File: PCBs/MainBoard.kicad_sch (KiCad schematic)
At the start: 37 parts, among them IC1 PASCO2V01BUMA1, J1 Conn_01x12_FPC_0.5mm, J4 SM06B-GHS-TB, J5 USB_C_Receptacle, SW1 SMD_4.6x2.8mm_h2.5mm, SW2 SMD_4.6x2.8mm_h2.5mm, SW3 PTH_RA_h7.5mm, U1 AP3012, U2 ESP32-S3-WROOM-1-N16R2, U5 AP2112K-3.3

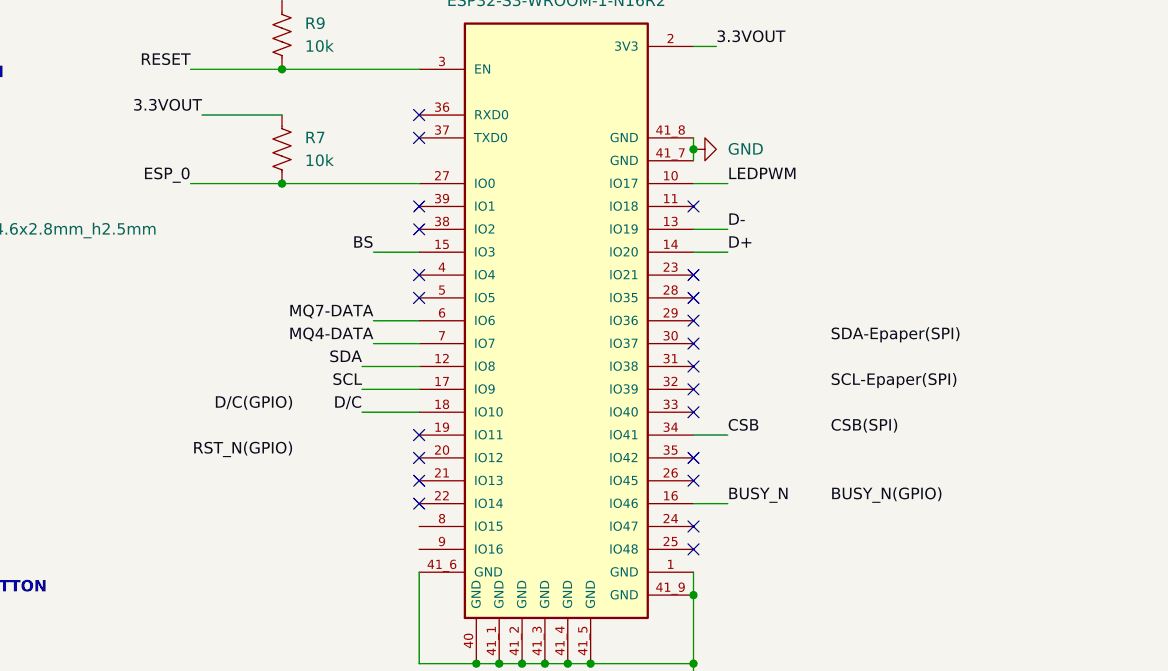
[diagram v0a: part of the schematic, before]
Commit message: Updated main board
Updated connections for Epaper discplay
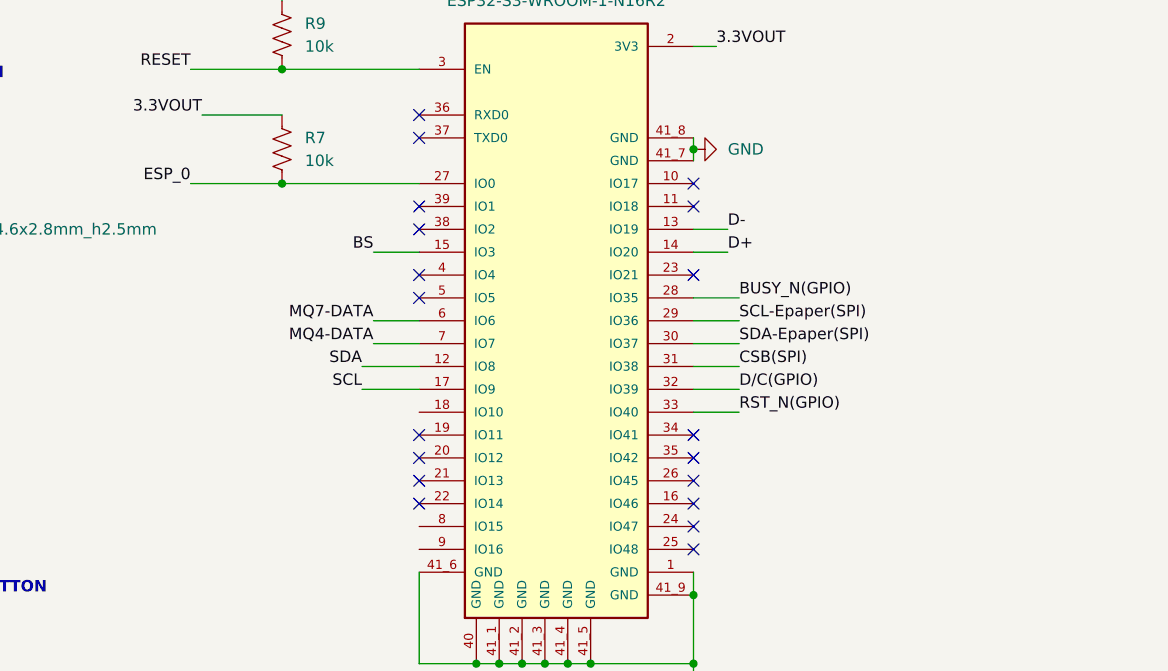
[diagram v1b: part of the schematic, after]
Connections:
- net BUSY_N(GPIO): now also U2.28 (IO35)
- net CSB(SPI): now also U2.31 (IO38)
- net D/C(GPIO): now also U2.32 (IO39)
- net RST_N(GPIO): now also U2.33 (IO40)
- net SCL-Epaper(SPI): now also U2.29 (IO36)
- net SDA-Epaper(SPI): now also U2.30 (IO37)
- net BUSY_N: no longer names the net of U2.16 (IO46)
- net CSB: no longer names the net of U2.34 (IO41)
- net D/C: no longer names the net of U2.18 (IO10)
- net LEDPWM: no longer names the net of U2.10 (IO17)
- no-connect marks 35 -> 32
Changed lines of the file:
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@@
   (no_connect (at 274.32 201.93))
   (no_connect (at 274.32 207.01))
+  (no_connect (at 123.19 173.99))
   (no_connect (at 92.71 140.97))
   (no_connect (at 92.71 133.35))
-  (no_connect (at 123.19 151.13))
   (no_connect (at 92.71 148.59))
   (no_connect (at 92.71 173.99))
   (no_connect (at 156.21 243.84))
   (no_connect (at 92.71 151.13))
-  (no_connect (at 123.19 156.21))
-  (no_connect (at 123.19 153.67))
   (no_connect (at 123.19 176.53))
   (no_connect (at 92.71 130.81))
@@
   (no_connect (at 123.19 171.45))
   (no_connect (at 156.21 248.92))
-  (no_connect (at 123.19 158.75))
-  (no_connect (at 123.19 161.29))
   (no_connect (at 123.19 140.97))
   (no_connect (at 241.3 196.85))
@@
   (no_connect (at 241.3 209.55))
   (no_connect (at 123.19 148.59))
+  (no_connect (at 123.19 166.37))
   (no_connect (at 274.32 204.47))
   (no_connect (at 92.71 143.51))
+  (no_connect (at 123.19 138.43))
   (no_connect (at 346.71 213.36))
   (no_connect (at 241.3 204.47))
@@
   (no_connect (at 123.19 168.91))
   (no_connect (at 123.19 179.07))
-  (no_connect (at 123.19 163.83))
   (wire (pts (xy 101.6 191.77) (xy 104.14 191.77))
     (stroke (width 0) (type default))
@@
     (stroke (width 0) (type default))
   )
+  (wire (pts (xy 128.27 158.75) (xy 123.19 158.75))
+    (stroke (width 0) (type default))
+  )
   (wire (pts (xy 123.19 133.35) (xy 123.19 134.62))
     (stroke (width 0) (type default))
@@
     (stroke (width 0) (type default))
   )
+  (wire (pts (xy 128.27 153.67) (xy 123.19 153.67))
+    (stroke (width 0) (type default))
+  )
   (wire (pts (xy 58.42 69.85) (xy 58.42 73.66))
     (stroke (width 0) (type default))
@@
     (stroke (width 0) (type default))
   )
+  (wire (pts (xy 128.27 156.21) (xy 123.19 156.21))
+    (stroke (width 0) (type default))
+  )
   (wire (pts (xy 260.35 66.04) (xy 260.35 64.77))
     (stroke (width 0) (type default))
   )
+  (wire (pts (xy 128.27 163.83) (xy 123.19 163.83))
+    (stroke (width 0) (type default))
+  )
   (wire (pts (xy 243.84 134.62) (xy 246.38 134.62))
     (stroke (width 0) (type default))
@@
     (stroke (width 0) (type default))
   )
-  (wire (pts (xy 127 138.43) (xy 123.19 138.43))
-    (stroke (width 0) (type default))
-  )
   (wire (pts (xy 321.31 58.42) (xy 339.09 58.42))
     (stroke (width 0) (type default))
@@
     (stroke (width 0) (type default))
   )
-  (wire (pts (xy 123.19 173.99) (xy 127 173.99))
-    (stroke (width 0) (type default))
-  )
   (wire (pts (xy 123.19 181.61) (xy 123.19 184.15))
     (stroke (width 0) (type default))
@@
     (stroke (width 0) (type default))
   )
-  (wire (pts (xy 86.36 163.83) (xy 92.71 163.83))
-    (stroke (width 0) (type default))
-  )
   (wire (pts (xy 266.7 134.62) (xy 273.05 134.62))
     (stroke (width 0) (type default))
@@
     (stroke (width 0) (type default))
   )
+  (wire (pts (xy 128.27 151.13) (xy 123.19 151.13))
+    (stroke (width 0) (type default))
+  )
   (wire (pts (xy 109.22 191.77) (xy 111.76 191.77))
     (stroke (width 0) (type default))
@@
     (stroke (width 0) (type default))
   )
-  (wire (pts (xy 123.19 166.37) (xy 127 166.37))
-    (stroke (width 0) (type default))
-  )
   (wire (pts (xy 227.33 54.61) (xy 240.03 54.61))
     (stroke (width 0) (type default))
@@
   )
   (wire (pts (xy 58.42 60.96) (xy 67.31 60.96))
+    (stroke (width 0) (type default))
+  )
+  (wire (pts (xy 128.27 161.29) (xy 123.19 161.29))
     (stroke (width 0) (type default))
   )
@@
     (effects (font (size 1.27 1.27)) (justify right bottom))
   )
-  (label "CSB" (at 127 166.37 0) (fields_autoplaced)
-    (effects (font (size 1.27 1.27)) (justify left bottom))
-  )
   (label "3.3VOUT" (at 127 223.52 180) (fields_autoplaced)
     (effects (font (size 1.27 1.27)) (justify right bottom))
@@
     (effects (font (size 1.27 1.27)) (justify right bottom))
   )
-  (label "D{slash}C(GPIO)" (at 78.74 163.83 180) (fields_autoplaced)
-    (effects (font (size 1.27 1.27)) (justify right bottom))
+  (label "CSB(SPI)" (at 128.27 158.75 0) (fields_autoplaced)
+    (effects (font (size 1.27 1.27)) (justify left bottom))
+  )
+  (label "D{slash}C(GPIO)" (at 128.27 161.29 0) (fields_autoplaced)
+    (effects (font (size 1.27 1.27)) (justify left bottom))
   )
   (label "SDA" (at 86.36 158.75 180) (fields_autoplaced)
@@
     (effects (font (size 1.27 1.27)) (justify left bottom))
   )
-  (label "BUSY_N(GPIO)" (at 138.43 173.99 0) (fields_autoplaced)
-    (effects (font (size 1.27 1.27)) (justify left bottom))
-  )
   (label "5V-IN" (at 336.55 200.66 180) (fields_autoplaced)
     (effects (font (size 1.27 1.27)) (justify right bottom))
@@
     (effects (font (size 1.27 1.27)) (justify left bottom))
   )
-  (label "BUSY_N" (at 127 173.99 0) (fields_autoplaced)
-    (effects (font (size 1.27 1.27)) (justify left bottom))
-  )
   (label "D-" (at 127 143.51 0) (fields_autoplaced)
     (effects (font (size 1.27 1.27)) (justify left bottom))
   )
-  (label "D{slash}C" (at 86.36 163.83 180) (fields_autoplaced)
-    (effects (font (size 1.27 1.27)) (justify right bottom))
-  )
   (label "SDA" (at 336.55 205.74 180) (fields_autoplaced)
     (effects (font (size 1.27 1.27)) (justify right bottom))
@@
     (effects (font (size 1.27 1.27)) (justify right bottom))
   )
-  (label "SDA-Epaper(SPI)" (at 138.43 156.21 0) (fields_autoplaced)
+  (label "SDA-Epaper(SPI)" (at 128.27 156.21 0) (fields_autoplaced)
     (effects (font (size 1.27 1.27)) (justify left bottom))
   )
@@
     (effects (font (size 1.27 1.27)) (justify right bottom))
   )
-  (label "SCL-Epaper(SPI)" (at 138.43 161.29 0) (fields_autoplaced)
+  (label "SCL-Epaper(SPI)" (at 128.27 153.67 0) (fields_autoplaced)
     (effects (font (size 1.27 1.27)) (justify left bottom))
   )
@@
     (effects (font (size 1.27 1.27)) (justify right bottom))
   )
-  (label "CSB(SPI)" (at 138.43 166.37 0) (fields_autoplaced)
-    (effects (font (size 1.27 1.27)) (justify left bottom))
-  )
   (label "D-" (at 67.31 60.96 0) (fields_autoplaced)
     (effects (font (size 1.27 1.27)) (justify left bottom))
@@
     (effects (font (size 1.27 1.27)) (justify left bottom))
   )
+  (label "BUSY_N(GPIO)" (at 128.27 151.13 0) (fields_autoplaced)
+    (effects (font (size 1.27 1.27)) (justify left bottom))
+  )
   (label "SCL" (at 336.55 208.28 180) (fields_autoplaced)
     (effects (font (size 1.27 1.27)) (justify right bottom))
@@
     (effects (font (size 1.27 1.27)) (justify right bottom))
   )
-  (label "RST_N(GPIO)" (at 78.74 168.91 180) (fields_autoplaced)
-    (effects (font (size 1.27 1.27)) (justify right bottom))
+  (label "RST_N(GPIO)" (at 128.27 163.83 0) (fields_autoplaced)
+    (effects (font (size 1.27 1.27)) (justify left bottom))
   )
   (label "RESET" (at 39.37 132.08 180) (fields_autoplaced)
@@
     (effects (font (size 1.27 1.27)) (justify right bottom))
   )
-  (label "LEDPWM" (at 127 138.43 0) (fields_autoplaced)
-    (effects (font (size 1.27 1.27)) (justify left bottom))
-  )
   (netclass_flag "" (length 2.54) (shape round) (at 86.36 49.53 0) (fields_autoplaced)

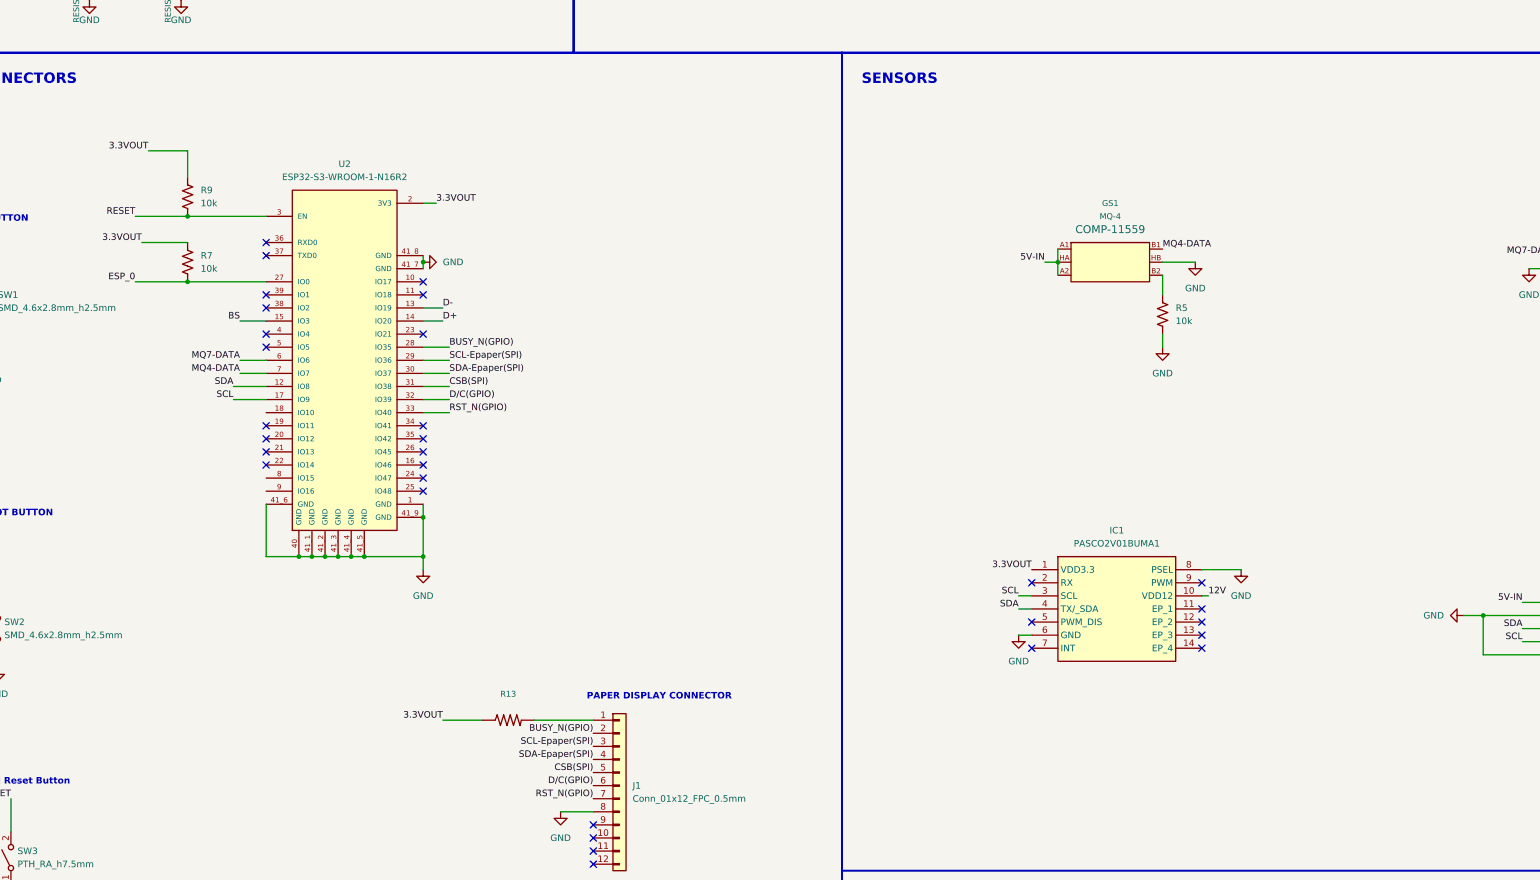
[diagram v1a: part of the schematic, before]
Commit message: Organizing PCB folder
Deleting old files and renaming files
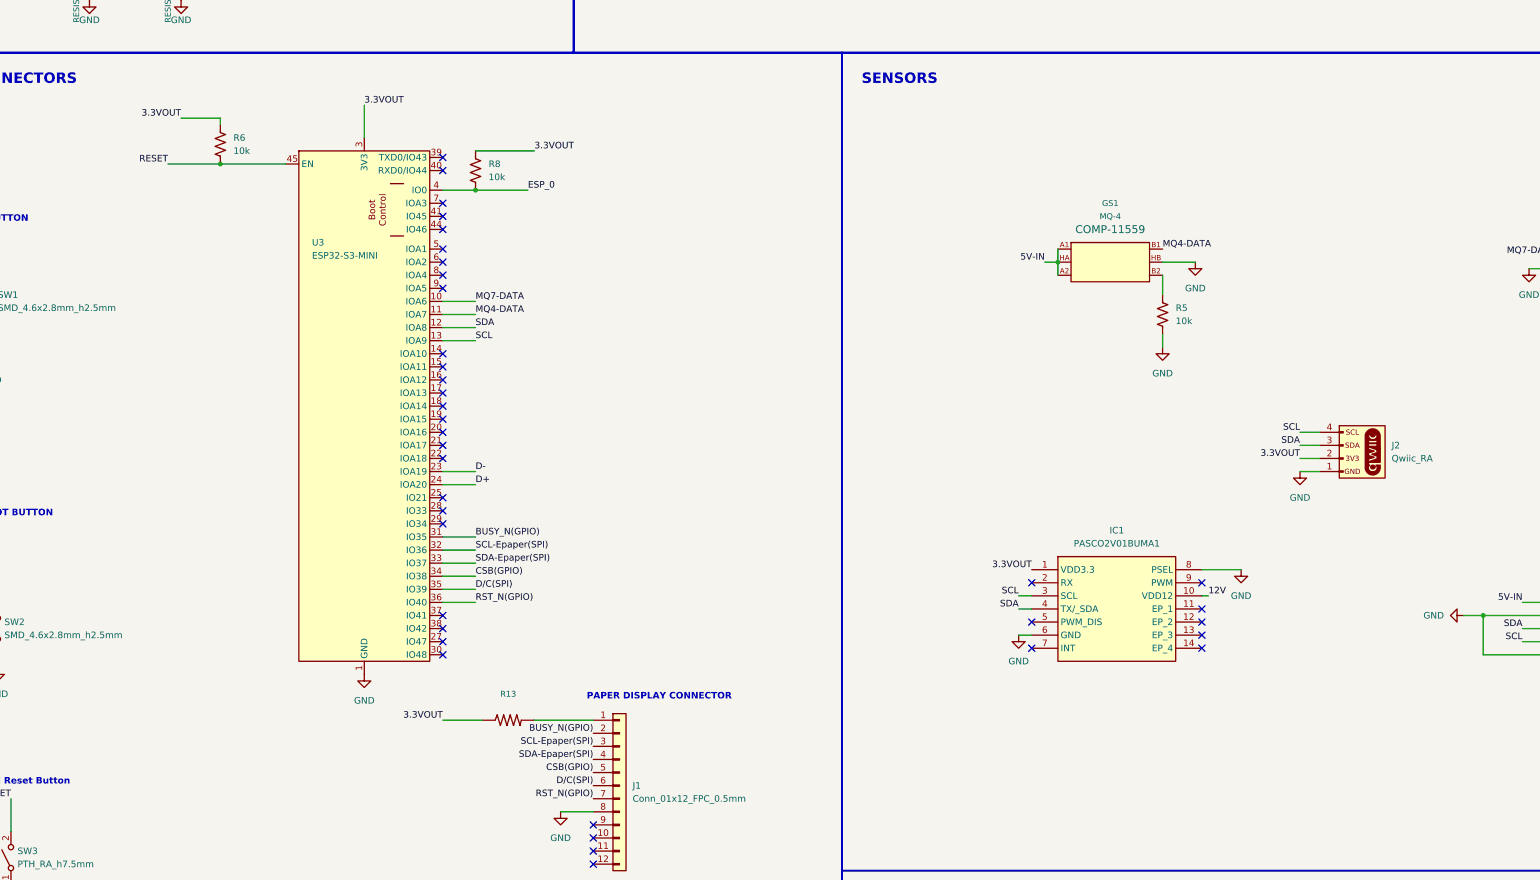
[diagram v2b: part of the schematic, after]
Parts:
- removed R7, R9: 10k, SparkFun-Resistor:R_0402_1005Metric, symbol SparkFun-Resistor:10k_0402
- removed U2: ESP32-S3-WROOM-1-N16R2, ESP32-S3-WROOM-1-N16R2:XCVR_ESP32-S3-WROOM-1-N16R2, symbol ESP32-S3-WROOM-1-N16R2:ESP32-S3-WROOM-1-N16R2
- added J2: Qwiic_RA, SparkFun-Connector:JST04_1MM_RA, symbol SparkFun-Connector:Qwiic_Right_Angle
- added R6, R8: 10k, SparkFun-Resistor:R_0402_1005Metric, symbol SparkFun-Resistor:10k_0402
- added U3: ESP32-S3-MINI, SparkFun-RF:ESP32-MINI, symbol SparkFun-RF:ESP32-S3-MINI
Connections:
- net 3.3VOUT: now also J2.2 (Pin_2), R6.1, R8.1, U3.3 (3V3)
- net BUSY_N(GPIO): now also U3.31 (IO35)
- net D+: now also U3.24 (IOA20)
- net D-: now also U3.23 (IOA19)
- net ESP_0: now also R8.2, U3.4 (IO0)
- net GND: now also J2.1 (Pin_1), U3.1 (GND), U3.2 (GND), U3.42 (GND), U3.43 (GND), U3.46 (GND), U3.47 (GND), U3.48 (GND), U3.49 (GND), U3.50 (GND), U3.51 (GND), U3.52 (GND), U3.53 (GND), U3.54 (GND), U3.55 (GND), U3.56 (GND), U3.57 (GND), U3.58 (GND), U3.59 (GND), U3.60 (GND), U3.61 (GND), U3.62 (GND), U3.63 (GND), U3.64 (GND), U3.65 (GND)
- net MQ4-DATA: now also U3.11 (IOA7)
- net MQ7-DATA: now also U3.10 (IOA6)
- net RESET: now also R6.2, U3.45 (EN)
- net RST_N(GPIO): now also U3.36 (IO40)
- net SCL: now also J2.4 (Pin_4), U3.13 (IOA9)
- net SCL-Epaper(SPI): now also U3.32 (IO36)
- net SDA: now also J2.3 (Pin_3), U3.12 (IOA8)
- net SDA-Epaper(SPI): now also U3.33 (IO37)
- net CSB(SPI) renamed CSB(GPIO)
- net CSB(GPIO): now also U3.34 (IO38)
- net D/C(GPIO) renamed D/C(SPI)
- net D/C(SPI): now also U3.35 (IO39)
- new net: J2.NC1 (NC), J2.NC2 (NC)
- no-connect marks 32 -> 38

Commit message: Updates in progress
Currently running through documentation provided. Home Air Quality Main Board Design Review google sheet for comments and what updates were preformed.
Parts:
- removed C1: 1.0UF-0402-16V-10%, 0402, symbol SparkFun-Capacitors:1.0UF-0402-16V-10%
- removed C8: 0.1UF-0402-16V-10%, 0402, symbol SparkFun-Capacitors:0.1UF-0402-16V-10%
- removed D3: White, SparkFun-LED:LED_0603_1608Metric, symbol SparkFun-LED:LED_White_0603
- removed R1, R2: RESISTOR0402-5.1k, 0402, symbol SparkFun-Resistors:RESISTOR0402
- removed R10, R4, R5, R6, R8: 10k, SparkFun-Resistor:R_0402_1005Metric, symbol SparkFun-Resistor:10k_0402
- removed R13: RESISTOR0402-120 ohm, 0402, symbol SparkFun-Resistors:RESISTOR0402
- removed R3: 10KOHM-0603-1_10W-1%, 0603, symbol SparkFun-Resistors:10KOHM-0603-1_10W-1%
- added C1, C2, C3: 0.1uF, SparkFun-Capacitor:C_0603_1608Metric, symbol SparkFun-Capacitor:0.1uF_0603_25V_20%
- added C10: 1.0uF, SparkFun-Capacitor:C_0603_1608Metric, symbol SparkFun-Capacitor:1.0uF_0603_16V_10%
- added D1, D3, D4: Red, SparkFun-LED:LED_0603_1608Metric, symbol SparkFun-LED:LED_Red_0603
- added JP1: Measure, SparkFun-Jumper:COMBO-JUMPER_2_NC_TRACE, symbol SparkFun-Jumper:Jumper_Measure
- added JP2, JP3, JP4: ~, SparkFun-Jumper:SMT-JUMPER_2_NC_TRACE_SILK, symbol SparkFun-Jumper:SolderJumper_2_Bridged
- added R1, R2: 5.1k, SparkFun-Resistor:R_0603_1608Metric, symbol SparkFun-Resistor:5.1k_0603
- added R10, R11, R3, R4, R8, R9: 10k, SparkFun-Resistor:R_0603_1608Metric, symbol SparkFun-Resistor:10k_0603
- added U1: TVS_ESD_USB, SparkFun-Semiconductor-Standard:SOT23-6, symbol SparkFun-DiscreteSemi:D_TVS_ESD_USB
- renumbered C9 to C11, C6 to C4, C10 to C5, C11 to C6, C12 to C7, C13 to C8, C14 to C9, D5 to D2, J5 to J1, J1 to J2, J2 to J3, L2 to L1, R14 to R5, R15 to R6, R16 to R7, SW3 to SW1, SW1 to SW2, SW2 to SW3, U3 to U2, U1 to U3, U5 to U4
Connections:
- net 3.3VOUT is gone; now on net +3.3V: C11.1, C4.1, IC1.1 (VDD3.3), J3.2 (Pin_2), L1.1, R5.1, U2.3 (3V3), U3.5 (IN), U4.5 (VOUT)
- net ESP_0 is gone; now on net +3.3V: SW3.2 (B), U2.4 (IO0)
- net TP_EN is gone; now on net +5V: U4.3 (EN)
- net D+: now also U1.6 (I/O4)
- net D-: now also U1.4 (I/O3)
- net GND: now also C1.1, C10.2, C2.2, C3.2, D1.1 (K), D3.1 (K), D4.1 (K), R1.2, R10.2, R2.2, R8.2, U1.2 (GND)
- net RESET: now also C1.2, R3.2
- net at A1.3 (B): now also R10.1
- net +3.3V: now reaches J2.1 (Pin_1)
- net +3.3V: now also C10.1, C3.1, JP4.2 (B), R3.1
- net at J1.A5 (CC1): now also R2.1
- net at J1.B5 (CC2): now also R1.1
- net at GS1.B2: now also R8.1
- net 12V renamed +12V
- net +12V: now also JP3.2 (B)
- net 5V-IN renamed +5V
- net +5V: now also C2.1, JP1.2 (B), JP2.2 (B), U1.5 (VCC); no longer J1.VBUS
- new net: JP4.1 (A), R11.1
- new net: J1.VBUS, JP1.1 (A)
- new net: D1.2 (A), R4.2
- new net: JP2.1 (A), R4.1
- new net: D4.2 (A), R11.2
- new net: D3.2 (A), R9.2
- new net: JP3.1 (A), R9.1
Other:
- moved on the sheet: C11, C4, C5, C6, C7, C8, C9, D2, J1, J2, L1, R5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
